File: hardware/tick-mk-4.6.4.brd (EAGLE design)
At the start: 96 x 53 mm, 40 parts, among them IC1 ATMEGA328P, IC2 DS3231, IC3 L7805, Y1 16MHz

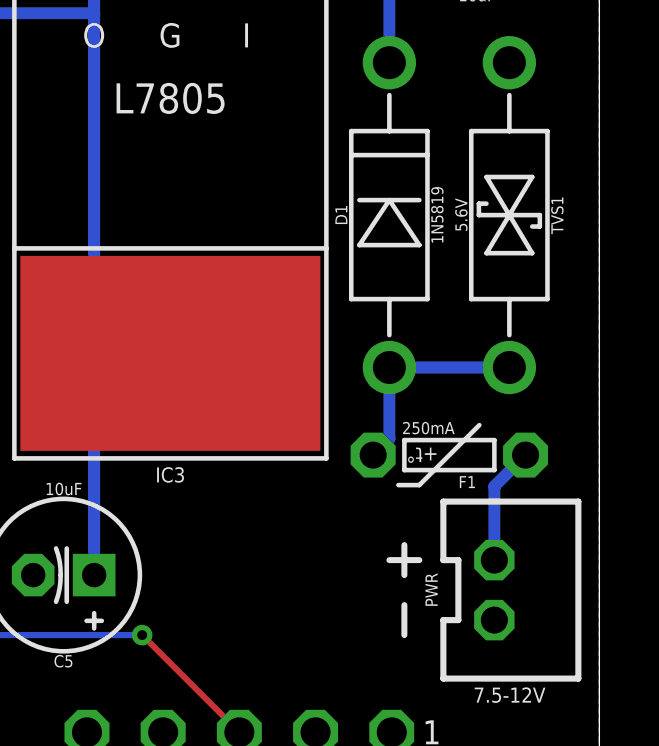
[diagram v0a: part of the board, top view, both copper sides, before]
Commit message: description update and further widening of bottom silk layer vector graphics in case that's oshapark's problem
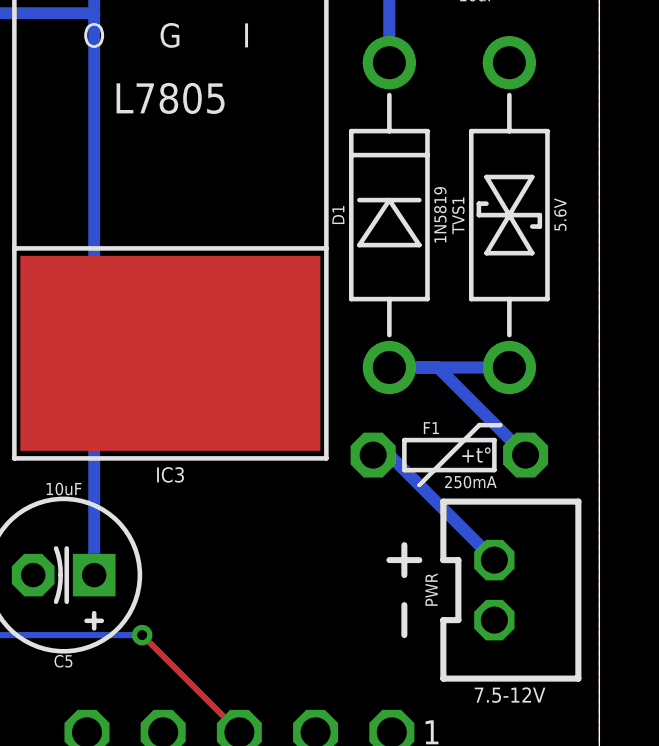
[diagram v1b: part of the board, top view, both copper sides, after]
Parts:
- turned F1 to 0 degrees
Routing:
- net N$4: track 7.14 -> 9.75 mm
- net N$7: track 3.93 -> 5.49 mm
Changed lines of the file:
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@@
 </element>
 <element name="TVS1" library="A_butts" package="DO-41-TVS-BI-10.16MM" value="5.6V" x="93" y="33" smashed="yes" rot="R270">
-<attribute name="NAME" x="94.4" y="33" size="0.4" layer="25" font="vector" ratio="11" rot="R270" align="bottom-center"/>
-<attribute name="VALUE" x="91.6" y="33" size="0.4" layer="21" font="vector" ratio="11" rot="R90" align="bottom-center"/>
-</element>
-<element name="F1" library="A_butts" package="PTC-PTH-5.08MM" value="250mA" x="91" y="25" smashed="yes" rot="R180">
-<attribute name="VALUE" x="90.3" y="25.7" size="0.4" layer="21" font="vector" ratio="12" rot="R180" align="top-center"/>
-<attribute name="NAME" x="91.6" y="24.3" size="0.4" layer="25" font="vector" ratio="12" rot="R180" align="bottom-center"/>
+<attribute name="NAME" x="91.5" y="33" size="0.4" layer="25" font="vector" ratio="11" rot="R90" align="bottom-center"/>
+<attribute name="VALUE" x="94.5" y="33" size="0.4" layer="21" font="vector" ratio="11" rot="R270" align="bottom-center"/>
+</element>
+<element name="F1" library="A_butts" package="PTC-PTH-5.08MM" value="250mA" x="91" y="25" smashed="yes">
+<attribute name="VALUE" x="91.7" y="24.3" size="0.4" layer="21" font="vector" ratio="12" align="top-center"/>
+<attribute name="NAME" x="90.4" y="25.7" size="0.4" layer="25" font="vector" ratio="12" align="bottom-center"/>
 </element>
 <element name="IC3" library="A_butts" package="TO220-IGO-THERMPAD" value="L7805" x="81.7" y="39.39" smashed="yes" rot="R180">
@@
 </element>
 <element name="D1" library="A_butts" package="DIODE-10.16MM" value="1N5819" x="89" y="33" smashed="yes" rot="R90">
-<attribute name="NAME" x="87.6" y="33" size="0.4" layer="25" font="vector" ratio="12" rot="R90" align="bottom-center"/>
-<attribute name="VALUE" x="90.4" y="33" size="0.4" layer="21" font="vector" ratio="12" rot="R90" align="top-center"/>
+<attribute name="NAME" x="87.5" y="33" size="0.4" layer="25" font="vector" ratio="12" rot="R90" align="bottom-center"/>
+<attribute name="VALUE" x="90.5" y="33" size="0.4" layer="21" font="vector" ratio="12" rot="R90" align="top-center"/>
 </element>
 <element name="RTC_BATTERY" library="A_butts" package="BATTCON_20MM_MINE" value="CR2030" x="10" y="31" smashed="yes">
@@
 <contactref element="F1" pad="P$2"/>
 <wire x1="89" y1="27.92" x2="93" y2="27.92" width="0.4" layer="16"/>
-<wire x1="88.46" y1="25" x2="89" y2="25.54" width="0.4" layer="16"/>
-<wire x1="89" y1="25.54" x2="89" y2="27.92" width="0.4" layer="16"/>
+<wire x1="93.54" y1="25" x2="90.62" y2="27.92" width="0.4" layer="16"/>
+<wire x1="90.62" y1="27.92" x2="89" y2="27.92" width="0.4" layer="16"/>
 </signal>
 <signal name="N$6">
@@
 <contactref element="PWR" pad="1"/>
 <contactref element="F1" pad="P$1"/>
-<wire x1="92.5" y1="21.5" x2="92.5" y2="23.96" width="0.4" layer="16"/>
-<wire x1="92.5" y1="23.96" x2="93.54" y2="25" width="0.4" layer="16"/>
+<wire x1="88.46" y1="25" x2="89" y2="25" width="0.4" layer="16"/>
+<wire x1="89" y1="25" x2="92.5" y2="21.5" width="0.4" layer="16"/>
 </signal>
 <signal name="N$5">
